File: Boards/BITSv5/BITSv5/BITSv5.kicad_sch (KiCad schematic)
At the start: 81 parts, among them J1 Conn_01x10_Pin, J2 USB_C_Receptacle_USB2.0, J3 Conn_01x07, Q1 Q_NMOS_GSD, Q2 Q_PMOS_GSD, SW3 SLIDE, U1 MCU_RaspberryPi_RP2040_RP2040, U10 USBLC6-2SC6, U2 W25Q128JVS, U3 MAX-M10S, U4 MAX25255AFDA/VY+, U6 XBee_SMT, U7 TPS2121RUXR, U8 LT6703CDC-3, U9 TVS1800DRVR, Y1 12MHz

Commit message: small update to BITSv5 for review
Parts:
- removed R6: 1M, Resistor_SMD:R_0603_1608Metric_Pad0.98x0.95mm_HandSolder, symbol Device:R
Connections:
- net GND: now also J2.S1 (SHIELD)
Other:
- moved on the sheet: C26, C27, U6

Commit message: xbee joint and bits updates
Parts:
- R17: value 51.1K -> 46.4K
- R18: value 1.05M -> 1.5M
- R19: value 154K -> 100K
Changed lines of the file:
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@@
       (effects (font (size 1.27 1.27)) (justify left))
     )
-    (property "Value" "1.05M" (at 259.08 33.02 0)
+    (property "Value" "1.5M" (at 259.08 33.02 0)
       (effects (font (size 1.27 1.27)) (justify left))
     )
@@
       (effects (font (size 1.27 1.27)) (justify left))
     )
-    (property "Value" "154K" (at 259.08 43.18 0)
+    (property "Value" "100K" (at 259.08 43.18 0)
       (effects (font (size 1.27 1.27)) (justify left))
     )
@@
       (effects (font (size 1.27 1.27)) (justify left))
     )
-    (property "Value" "51.1K" (at 45.72 262.89 0)
-      (effects (font (size 1.27 1.27)) (justify left))
-    )
+    (property "Value" "46.4K" (at 45.72 262.89 0)
+      (effects (font (size 1.27 1.27)) (justify left))
+    )

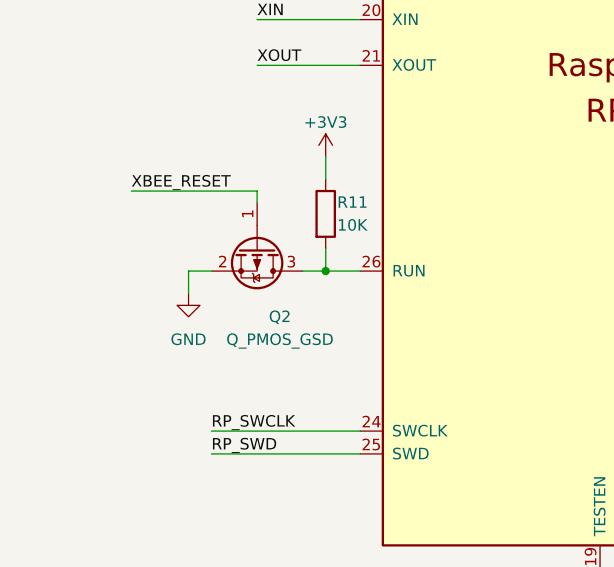
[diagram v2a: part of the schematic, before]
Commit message: added button to BITS5
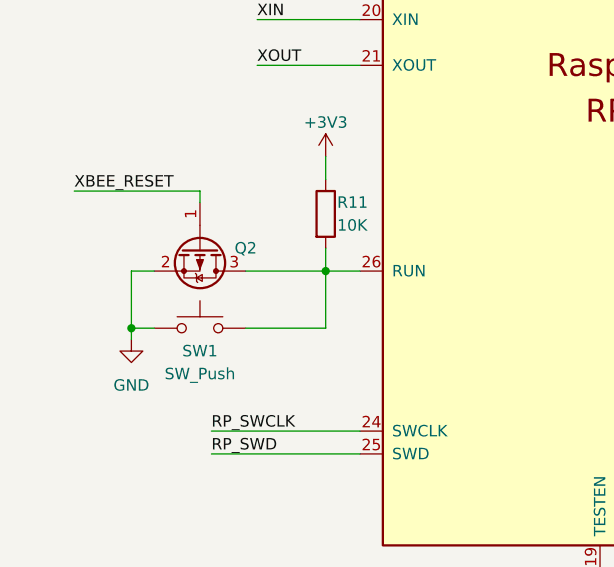
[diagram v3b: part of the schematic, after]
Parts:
- added SW1: SW_Push, Button_Switch_SMD:SW_Push_1P1T-SH_NO_CK_KMR2xxG, symbol Switch:SW_Push
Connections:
- net GND: now also SW1.1
- net at Q2.3 (D), R11.2, U1.26 (RUN): now also SW1.2
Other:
- moved on the sheet: Q2
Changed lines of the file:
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@@
   (junction (at 49.53 21.59) (diameter 0) (color 0 0 0 0)
   )
+  (junction (at 20.32 111.76) (diameter 0) (color 0 0 0 0)
+  )
   (junction (at 142.24 21.59) (diameter 0) (color 0 0 0 0)
   )
@@
     (stroke (width 0) (type default))
   )
-  (wire (pts (xy 29.21 105.41) (xy 26.67 105.41))
+  (wire (pts (xy 22.86 105.41) (xy 20.32 105.41))
     (stroke (width 0) (type default))
   )
@@
     (stroke (width 0) (type default))
   )
+  (wire (pts (xy 33.02 111.76) (xy 41.91 111.76))
+    (stroke (width 0) (type default))
+  )
   (wire (pts (xy 287.02 191.77) (xy 297.18 191.77))
     (stroke (width 0) (type default))
@@
     (stroke (width 0) (type default))
   )
-  (wire (pts (xy 34.29 96.52) (xy 20.32 96.52))
+  (wire (pts (xy 27.94 96.52) (xy 13.97 96.52))
     (stroke (width 0) (type default))
   )
@@
     (stroke (width 0) (type default))
   )
-  (wire (pts (xy 39.37 105.41) (xy 41.91 105.41))
+  (wire (pts (xy 33.02 105.41) (xy 41.91 105.41))
     (stroke (width 0) (type default))
   )
@@
     (stroke (width 0) (type default))
   )
+  (wire (pts (xy 41.91 111.76) (xy 41.91 105.41))
+    (stroke (width 0) (type default))
+  )
   (wire (pts (xy 222.25 177.8) (xy 222.25 179.07))
     (stroke (width 0) (type default))
@@
     (stroke (width 0) (type dash_dot))
   )
-  (wire (pts (xy 26.67 105.41) (xy 26.67 107.95))
+  (wire (pts (xy 20.32 105.41) (xy 20.32 111.76))
     (stroke (width 0) (type default))
   )
@@
     (stroke (width 0) (type default))
   )
-  (wire (pts (xy 34.29 96.52) (xy 34.29 97.79))
+  (wire (pts (xy 27.94 96.52) (xy 27.94 97.79))
     (stroke (width 0) (type default))
   )
@@
     (stroke (width 0) (type default))
   )
+  (wire (pts (xy 20.32 113.03) (xy 20.32 111.76))
+    (stroke (width 0) (type default))
+  )
   (wire (pts (xy 248.92 255.27) (xy 248.92 256.54))
     (stroke (width 0) (type default))
@@
     (stroke (width 0) (type default))
   )
+  (wire (pts (xy 20.32 111.76) (xy 22.86 111.76))
+    (stroke (width 0) (type default))
+  )
   (wire (pts (xy 363.22 33.02) (xy 364.49 33.02))
     (stroke (width 0) (type default))
@@
     (effects (font (size 1.27 1.27)) (justify left bottom))
   )
-  (label "XBEE_RESET" (at 20.32 96.52 0) (fields_autoplaced)
+  (label "XBEE_RESET" (at 13.97 96.52 0) (fields_autoplaced)
     (effects (font (size 1.27 1.27)) (justify left bottom))
   )
@@
     )
   )
-  (symbol (lib_id "power:GND") (at 26.67 107.95 0) (unit 1)
+  (symbol (lib_id "power:GND") (at 20.32 113.03 0) (unit 1)
     (in_bom yes) (on_board yes) (dnp no) (fields_autoplaced)
-    (property "Reference" "#PWR038" (at 26.67 114.3 0)
+    (property "Reference" "#PWR038" (at 20.32 119.38 0)
       (effects (font (size 1.27 1.27)) hide)
     )
-    (property "Value" "GND" (at 26.67 113.03 0)
+    (property "Value" "GND" (at 20.32 118.11 0)
       (effects (font (size 1.27 1.27)))
     )
-    (property "Footprint" "" (at 26.67 107.95 0)
+    (property "Footprint" "" (at 20.32 113.03 0)
       (effects (font (size 1.27 1.27)) hide)
     )
-    (property "Datasheet" "" (at 26.67 107.95 0)
+    (property "Datasheet" "" (at 20.32 113.03 0)
       (effects (font (size 1.27 1.27)) hide)
     )
@@
     )
   )
-  (symbol (lib_id "Device:Q_PMOS_GSD") (at 34.29 102.87 270) (unit 1)
+  (symbol (lib_id "Device:Q_PMOS_GSD") (at 27.94 102.87 270) (unit 1)
     (in_bom yes) (on_board yes) (dnp no)
-    (property "Reference" "Q2" (at 36.83 110.49 90)
+    (property "Reference" "Q2" (at 33.02 102.87 90)
       (effects (font (size 1.27 1.27)))
     )
-    (property "Value" "Q_PMOS_GSD" (at 36.83 113.03 90)
-      (effects (font (size 1.27 1.27)))
+    (property "Value" "Q_PMOS_GSD" (at 30.48 90.17 90)
+      (effects (font (size 1.27 1.27)) hide)
     )
-    (property "Footprint" "Package_TO_SOT_SMD:SOT-23" (at 36.83 107.95 0)
+    (property "Footprint" "Package_TO_SOT_SMD:SOT-23" (at 30.48 107.95 0)
       (effects (font (size 1.27 1.27)) hide)
     )
-    (property "Datasheet" "~" (at 34.29 102.87 0)
+    (property "Datasheet" "~" (at 27.94 102.87 0)
       (effects (font (size 1.27 1.27)) hide)
     )
@@
         )
       )
+    )
+  )
+  (symbol (lib_id "Switch:SW_Push") (at 27.94 111.76 0) (unit 1)
+    (in_bom yes) (on_board yes) (dnp no)
+    (property "Reference" "SW1" (at 27.94 114.3 0)
+      (effects (font (size 1.27 1.27)))
+    )
+    (property "Value" "SW_Push" (at 27.94 116.84 0)
+      (effects (font (size 1.27 1.27)))
+    )
+    (property "Footprint" "Button_Switch_SMD:SW_Push_1P1T-SH_NO_CK_KMR2xxG" (at 27.94 106.68 0)
+      (effects (font (size 1.27 1.27)) hide)
+    )
+    (property "Datasheet" "~" (at 27.94 106.68 0)
+      (effects (font (size 1.27 1.27)) hide)
+    )
+    (pin "1")
+    (pin "2")
+    (instances
+      (project "BITSv5"
+        (path "/55a258d3-b7da-466a-a6cc-38d8142826fc"
+          (reference "SW1") (unit 1)
+        )
+      )

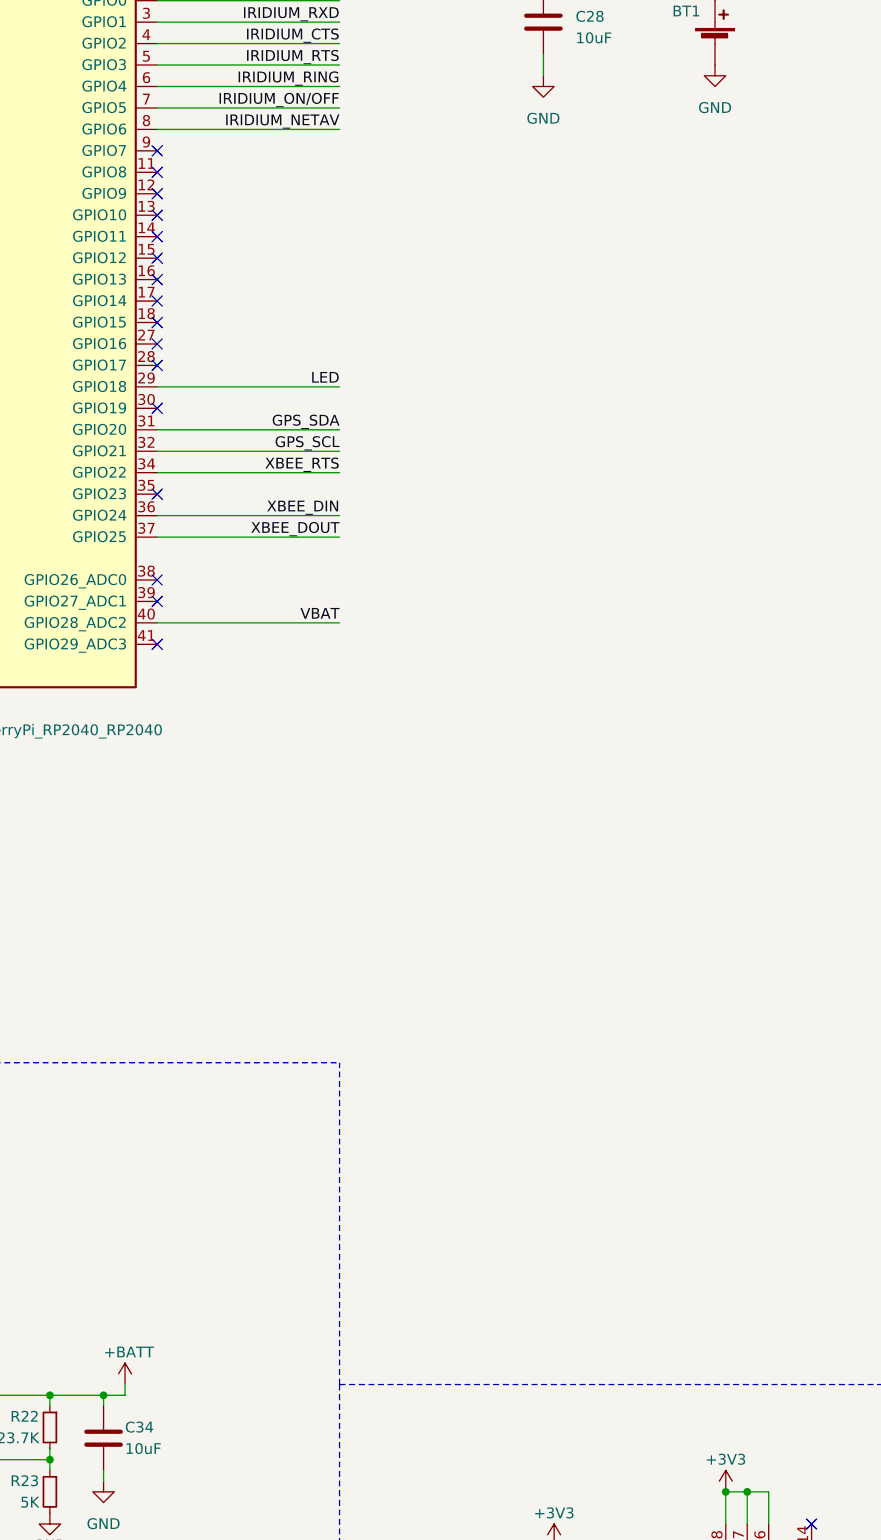
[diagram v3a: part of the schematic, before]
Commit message: BITSv5 added additional Xbee connector
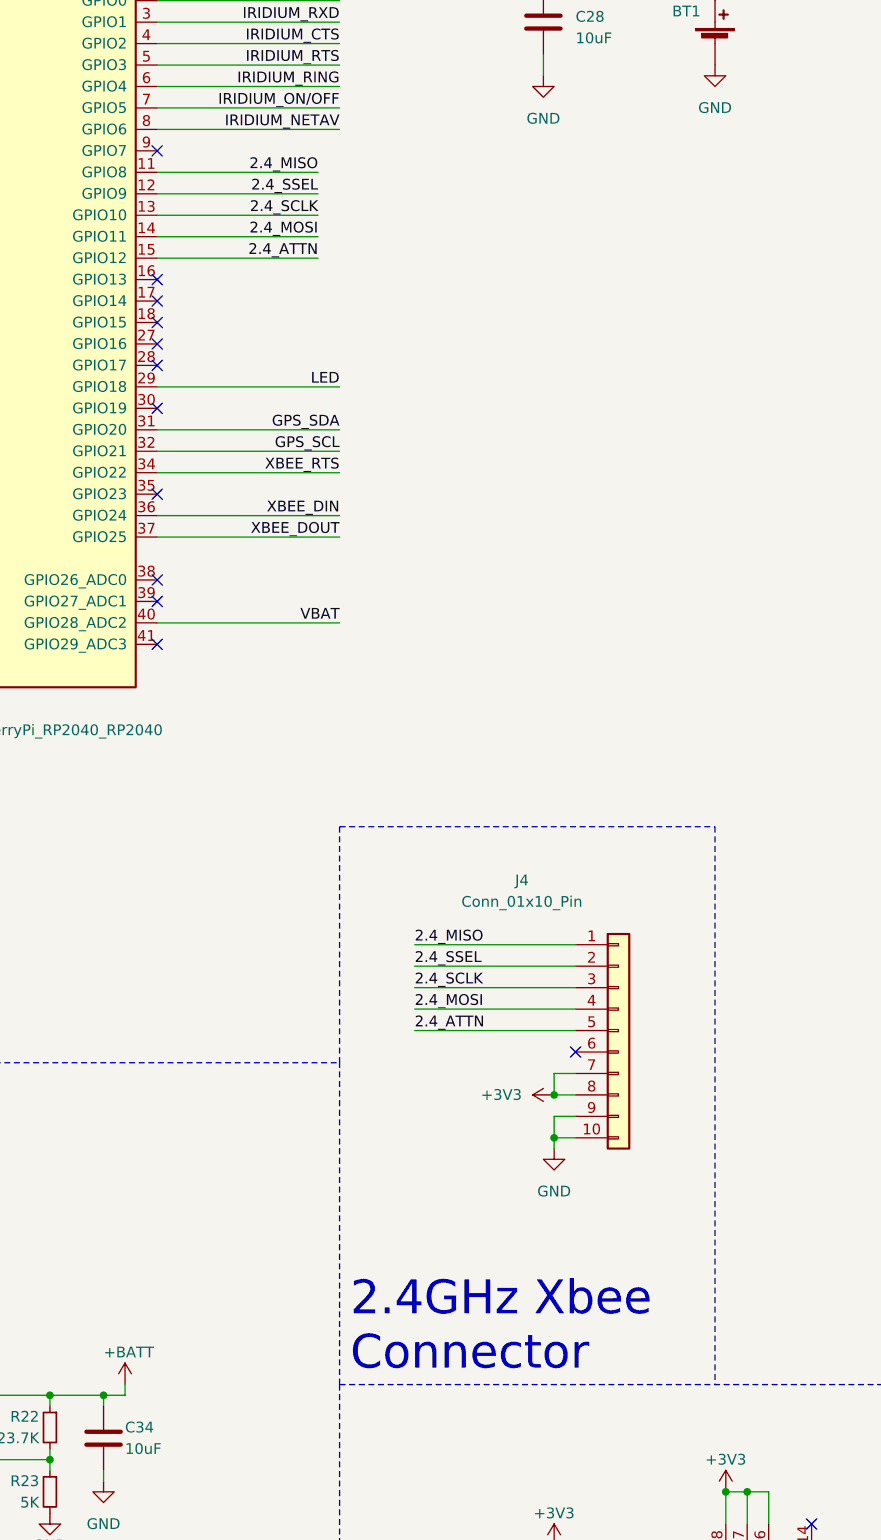
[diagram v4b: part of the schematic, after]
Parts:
- added J4: Conn_01x10_Pin, Connector_Molex:Molex_PicoBlade_53048-1010_1x10_P1.25mm_Horizontal, symbol Connector_Generic:Conn_01x10
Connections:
- net +3V3: now also J4.7 (Pin_7), J4.8 (Pin_8)
- net GND: now also J4.10 (Pin_10), J4.9 (Pin_9)
- net 2.4_MISO: now reaches U1.11 (GPIO8)
- net 2.4_MISO: now also J4.1 (Pin_1)
- net 2.4_SSEL: now reaches U1.12 (GPIO9)
- net 2.4_SSEL: now also J4.2 (Pin_2)
- net 2.4_SCLK: now reaches U1.13 (GPIO10)
- net 2.4_SCLK: now also J4.3 (Pin_3)
- net 2.4_MOSI: now reaches U1.14 (GPIO11)
- net 2.4_MOSI: now also J4.4 (Pin_4)
- net 2.4_ATTN: now reaches U1.15 (GPIO12)
- net 2.4_ATTN: now also J4.5 (Pin_5)
- no-connect marks 51 -> 47
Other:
- note added: "2.4GHz Xbee Connector"

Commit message: bits v5 w/ dorji radio
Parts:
- removed C17, C18, C19, C20, C21, C22: 22uF, Capacitor_SMD:C_0603_1608Metric_Pad1.08x0.95mm_HandSolder, symbol Device:C
- removed C23, C24: 0.1uF, Capacitor_SMD:C_0402_1005Metric_Pad0.74x0.62mm_HandSolder, symbol Device:C
- removed C26: 100pF, Capacitor_SMD:C_0603_1608Metric_Pad1.08x0.95mm_HandSolder, symbol Device:C
- removed C27: 1uF, Capacitor_SMD:C_0603_1608Metric_Pad1.08x0.95mm_HandSolder, symbol Device:C
- removed C28: 10uF, Capacitor_SMD:C_0603_1608Metric_Pad1.08x0.95mm_HandSolder, symbol Device:C
- removed C31: 0.1uF, Capacitor_SMD:C_0603_1608Metric_Pad1.08x0.95mm_HandSolder, symbol Device:C_Small
- removed J3: Conn_01x07, Connector_PinSocket_2.54mm:PinSocket_1x07_P2.54mm_Vertical, symbol Connector_Generic:Conn_01x07
- removed J4: Conn_01x10_Pin, Connector_Molex:Molex_PicoBlade_53048-1010_1x10_P1.25mm_Horizontal, symbol Connector_Generic:Conn_01x10
- removed L1, L2: 0.47uH, Inductor_SMD:L_1008_2520Metric_Pad1.43x2.20mm_HandSolder, symbol Device:L
- removed Q2: Q_PMOS_GSD, Package_TO_SOT_SMD:SOT-23, symbol Device:Q_PMOS_GSD
- removed R11: 10K, Resistor_SMD:R_0603_1608Metric_Pad0.98x0.95mm_HandSolder, symbol Device:R
- removed U4: MAX25255AFDA/VY+, BITSv5:21-100477_90-100168_MXM, symbol BITSv5:MAX25255DAFDG_VY+
- removed U6: XBee_SMT, BITSv5:XCVR_XBP9X-DMUS-001, symbol BITSv5:XBP9X-DMUS-001
- added AE2: Antenna, BITSv5:ANT_0915AT43A0026E_JOT, symbol Device:Antenna
- added BT2: 3V, BITSv5:SEIKO_ML414H_IV01E, symbol Device:Battery_Cell
- added C17, C23: 4.7pF, Capacitor_SMD:C_0603_1608Metric, symbol Device:C_Small
- added C18, C21: 470pF, Capacitor_SMD:C_0603_1608Metric, symbol Device:C_Small
- added C19, C24: 10nF, Capacitor_SMD:C_0603_1608Metric, symbol Device:C_Small
- added C20: 100uF, Capacitor_SMD:C_1206_3216Metric, symbol Device:C_Small
- added C22, C42: 100nF, Capacitor_SMD:C_0603_1608Metric, symbol Device:C_Small
- added C26: 10uF, Capacitor_SMD:C_0603_1608Metric, symbol Device:C_Small
- added C27, C39, C40, C41: 1uF, Capacitor_SMD:C_0603_1608Metric, symbol Device:C_Small
- added C28, C38: 15uF, Capacitor_SMD:C_1206_3216Metric, symbol Device:C_Small
- added C43: 200nF, Capacitor_SMD:C_0603_1608Metric, symbol Device:C_Small
- added D2: 0.5A/40V/240mV, Diode_SMD:D_SOD-123F, symbol Device:D_Schottky_Small
- added H1, H2, H4: M2, MountingHole:MountingHole_2.2mm_M2_Pad, symbol Mechanical:MountingHole
- added H3: M2, MountingHole:MountingHole_2.2mm_M2_Pad, symbol Mechanical:MountingHole_Pad
- added J3: SOICbite, BITSv5:SOIC_clipProgSmall, symbol Connector:Conn_01x08_Socket
- added L1, L2: 2.2uH, Inductor_SMD:L_1210_3225Metric, symbol Device:L_Small
- added L3, L4: 3.3uH, Inductor_SMD:L_1210_3225Metric, symbol Device:L_Small
- added R11, R29, R33: 100K, Resistor_SMD:R_0603_1608Metric, symbol Device:R_Small
- added R13: 100m, Resistor_SMD:R_0603_1608Metric, symbol Device:R_Small
- added R14: 3.3K, Resistor_SMD:R_0603_1608Metric, symbol Device:R_Small
- added R27: 22.1K, Resistor_SMD:R_0603_1608Metric, symbol Device:R_Small
- added R32: 34.8K, Resistor_SMD:R_0603_1608Metric, symbol Device:R_Small
- added R34: 15K, Resistor_SMD:R_0603_1608Metric, symbol Device:R_Small
- added R6: 10K, Resistor_SMD:R_0603_1608Metric, symbol Device:R_Small
- added U11: MS5607-02BA, Package_LGA:LGA-8_3x5mm_P1.25mm, symbol Sensor_Pressure:MS5607-02BA
- added U4: DRF1262TL, BITSv5:DRF1262TL, symbol BITSv5:DRF1262TL
- added U5: LT8653SIV-PBF, BITSv5:LT8653SIV-PBF, symbol BITSv5:LT8653SIV-PBF
- added U7: MAX6747KA29+T, 21-0078H_MXM, symbol BITSv5:MAX6747KA29+T
- C1, C10, C11, C2, C3, C32, C4, C5, C6, C7, C8, C9: footprint Capacitor_SMD:C_0402_1005Metric_Pad0.74x0.62mm_HandSolder -> Capacitor_SMD:C_0402_1005Metric; symbol Device:C -> Device:C_Small
- C12, C13, C14, C37: footprint Capacitor_SMD:C_0603_1608Metric_Pad1.08x0.95mm_HandSolder -> Capacitor_SMD:C_0402_1005Metric; symbol Device:C -> Device:C_Small
- C15: value 0.1uF -> 4.7uF; footprint Capacitor_SMD:C_0603_1608Metric_Pad1.08x0.95mm_HandSolder -> Capacitor_SMD:C_0603_1608Metric
- C16: value 4.7uF -> 47uF; footprint Capacitor_SMD:C_0603_1608Metric_Pad1.08x0.95mm_HandSolder -> Capacitor_SMD:C_1206_3216Metric
- C25: value 2.2uF -> 1uF; footprint Capacitor_SMD:C_0603_1608Metric_Pad1.08x0.95mm_HandSolder -> Capacitor_SMD:C_0603_1608Metric
- C29, C30: value 4.7uF -> 100nF; footprint Capacitor_SMD:C_0603_1608Metric_Pad1.08x0.95mm_HandSolder -> Capacitor_SMD:C_0603_1608Metric
- C33, C34, C35, C36: footprint Capacitor_SMD:C_0603_1608Metric_Pad1.08x0.95mm_HandSolder -> Capacitor_SMD:C_0603_1608Metric; symbol Device:C -> Device:C_Small
- J1: footprint Connector_Molex:Molex_PicoBlade_53048-1010_1x10_P1.25mm_Horizontal -> Connector_Molex:Molex_PicoBlade_53261-1071_1x10-1MP_P1.25mm_Horizontal
- J2: footprint Connector_USB:USB_C_Receptacle_GCT_USB4085 -> Connector_USB:USB_C_Receptacle_GCT_USB4105-xx-A_16P_TopMnt_Horizontal
- R1, R2: value 27Ω -> 27; footprint Resistor_SMD:R_0402_1005Metric_Pad0.72x0.64mm_HandSolder -> Resistor_SMD:R_0402_1005Metric; symbol Device:R -> Device:R_Small
- R10: value 10K -> 100m; footprint Resistor_SMD:R_0603_1608Metric_Pad0.98x0.95mm_HandSolder -> Resistor_SMD:R_0603_1608Metric
- R12, R21, R24, R4: footprint Resistor_SMD:R_0603_1608Metric_Pad0.98x0.95mm_HandSolder -> Resistor_SMD:R_0603_1608Metric; symbol Device:R -> Device:R_Small
- R15, R16, R22, R23, R9: footprint Resistor_SMD:R_0603_1608Metric_Pad0.98x0.95mm_HandSolder -> Resistor_SMD:R_0603_1608Metric
- R17: value 46.4K -> 44.2K; footprint Resistor_SMD:R_0603_1608Metric_Pad0.98x0.95mm_HandSolder -> Resistor_SMD:R_0603_1608Metric; symbol Device:R -> Device:R_Small
- R18, R19, R20: footprint Resistor_SMD:R_0603_1608Metric_Pad0.98x0.95mm_HandSolder -> Resistor_SMD:R_0402_1005Metric; symbol Device:R -> Device:R_Small
- R3: value 10K -> DNF; footprint Resistor_SMD:R_0603_1608Metric_Pad0.98x0.95mm_HandSolder -> Resistor_SMD:R_0603_1608Metric; symbol Device:R -> Device:R_Small
- R5: footprint Resistor_SMD:R_0402_1005Metric_Pad0.72x0.64mm_HandSolder -> Capacitor_SMD:C_0402_1005Metric; symbol Device:R -> Device:R_Small
- R7, R8: symbol Device:R -> Device:R_Small
- U1: symbol RP2040_minimal-cache:MCU_RaspberryPi_RP2040_RP2040 -> BITSv5:MCU_RaspberryPi_RP2040
- U10: footprint BITSv5:SOT23-6L_STM-M -> SOT23-6L_STM; symbol USBLC6-2SC6:USBLC6-2SC6 -> BITSv5:USBLC6-2SC6
- U2: footprint Package_SO:SOIC-8_5.23x5.23mm_P1.27mm -> BITSv5:WSON_128JVPIQ_WIN
- U6: renamed from U7; symbol TPS2121:TPS2121RUXR -> BITSv5:TPS2121RUXR
- Y1: symbol Device:Crystal_GND24 -> Device:Crystal_GND24_Small
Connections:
- net 2.4_ATTN is gone; now on net IRIDIUM_TXD: U1.15 (GPIO12)
- net GPS_SDA is gone; now on net SDA: R21.2, U1.31 (GPIO20), U3.16 (SDA)
- net +3V3: now also C29.1, R9.1, C28.1, C39.1, C41.1, D2.2 (A), L3.1, R11.1, R6.1, U11.1 (VDD), U11.2 (PS), U7.5 (WDS), U7.8 (VCC); no longer U3.6 (V_BCKP)
- net +5V: now also C26.1, C27.1, C38.1, L4.1, R13.1, U4.6 (VDD), U4.7 (VDD); no longer R9.1
- net GND: now also C13.2, C14.2, C15.2, C25.2, C29.2, C30.2, BT2.2 (-), C17.2, C18.2, C19.2, C20.2, C21.2, C22.2, C23.2, C24.2, C26.2, C27.2, C28.2, C38.2, C39.2, C40.2, C41.2, C42.2, C43.2, H3.1, J3.8 (Pin_8), R34.2, U11.3 (GND), U11.4 (CSB), U11.5 (CSB), U4.15 (GND), U4.17 (GND), U4.2 (GND), U4.4 (GND), U4.5 (GND), U5.21 (GND), U7.4 (GND); no longer C13.1, C14.1, C15.1, C25.1, C29.1, C30.1
- net IRIDIUM_NETAV: now also U1.6 (GPIO4); no longer U1.8 (GPIO6)
- net IRIDIUM_RING: now also U1.7 (GPIO5); no longer U1.6 (GPIO4)
- net IRIDIUM_TXD: no longer U1.2 (GPIO0)
- net LED: now also U1.2 (GPIO0); no longer U1.29 (GPIO18)
- net LVC_CUTOFF: now also U5.18 (EN/UV)
- net RP_SWCLK: now also J3.1 (Pin_1)
- net RP_SWD: now also J3.2 (Pin_2)
- net VCC: now also C15.1, C22.1, U5.19 (VIN), U5.20 (VIN), U5.5 (SYNC); no longer C15.2, C16.1, C29.2
- net at R5.1, Y1.1: now also C14.1; no longer C14.2
- net SDA: now reaches R9.2
- net SDA: now also U11.7 (SDI/SDA)
- net at SW1.2: now also C30.1, U7.1 (*MR); no longer U1.26 (RUN)
- net at R10.2: now also C20.1, L2.1, L3.2, R33.1, U5.10 (BIAS), U5.15 (FB2)
- net WATCHDOG: now reaches U1.16 (GPIO13)
- net WATCHDOG: now also U7.6 (WDI)
- net DRF_CLK: now reaches U1.38 (GPIO26_ADC0)
- net DRF_CLK: now also U4.13 (SCK)
- net DRF_MOSI: now reaches U1.39 (GPIO27_ADC1)
- net DRF_MOSI: now also U4.12 (MOSI)
- net 2.4_MISO renamed DRF_TXEN
- net DRF_TXEN: now also U4.3 (TXEN)
- net 2.4_MOSI renamed DRF_BUSY
- net DRF_BUSY: now also U4.9 (BUSY)
- net 2.4_SCLK renamed DRF_DIO1
- net DRF_DIO1: now also U4.8 (DIO1)
- net 2.4_SSEL renamed DRF_SW
- net DRF_SW: now also U4.1 (SW)
- net GPS_SCL renamed SCL
- net SCL: now also R6.2, U11.8 (SCLK)
- net IRIDIUM_ON/OFF renamed RESET
- net RESET: now also U1.26 (RUN), R11.2, U4.10 (RST), U7.7 (*RESET); no longer U1.7 (GPIO5)
- net VBAT: no longer names the net of U1.40 (GPIO28_ADC2)
- net XBEE_DIN renamed DRF_MISO
- net DRF_MISO: now also U4.11 (MISO)
- net XBEE_DOUT renamed DRF_CS
- net DRF_CS: now also U4.14 (NSS)
- net XBEE_RTS: no longer names the net of U1.34 (GPIO22)
- net XIN: no longer names the net of U1.20 (XIN), Y1.3
- net XIN: now also C13.1; no longer C13.2
- net XOUT: no longer names the net of R5.2, U1.21 (XOUT)
- new net: C17.1, R27.2, U5.11 (VC1)
- new net: D2.1 (K), R14.1
- new net: C25.1, U5.9 (VCC)
- new net: U3.10 (GND), U3.12 (GND)
- new net: BT2.1 (+), C40.1, R14.2, U3.6 (V_BCKP)
- new net: C42.1, U7.2 (SWT)
- new net: C43.1, U7.3 (SRT)
- new net: C18.1, R27.1
- new net: C21.1, R32.1
- new net: C23.1, R32.2, U5.16 (VC2)
- new net: C16.1, L1.1, L4.2, R13.2, R29.1, U5.12 (FB1)
- new net: C24.1, U5.14 (SS2)
- new net: AE2.1 (A), U4.16 (ANT)
- new net: R34.1, U5.17 (RT)
- new net: C19.1, U5.13 (SS1)
- new net: R33.2, U5.3 (PG2)
- new net: R29.2, U5.4 (PG1)
- new net: L1.2, U5.7 (SW1)
- new net: L2.2, U5.8 (SW2)
- no-connect marks 47 -> 34
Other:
- note added: "5V / 3.3V Buck Regulator"
- note added: "MCU"
- note added: "Power Multiplexer"
- note added: "Pressure and Temp. Sensor"
- note added: "Radio"
- note added: "RockBlock"
- note added: "SOICbite"
- note added: "USB C Plug"
- note added: "Voltage Clamps"
- note added: "Watchdog"
- note removed: "2.4GHz Xbee Connector"
- note removed: "Crystal"
- note removed: "Debug Headers"
- note removed: "Dual Buck Regulator"
- note removed: "Power Mux"
- note removed: "RockBlock Connector"
- note removed: "USB C Port"
- note removed: "XBee Pro SX 900"
- moved on the sheet: AE1, BT1, C1, C10, C11, C12, C13, C14, C2, C3, C32, C33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

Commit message: ordered new joint and bits
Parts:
- C17, C23: value 4.7pF -> 10pF
- C20: value 100uF -> 47uF
- C43: value 200nF -> 220nF
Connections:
- new net: U3.10 (GND), U3.12 (GND)
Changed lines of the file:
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@@
       (effects (font (size 1.27 1.27)))
     )
-    (property "Value" "4.7pF" (at 314.96 57.15 0)
+    (property "Value" "10pF" (at 314.96 57.15 0)
       (effects (font (size 1.27 1.27)))
     )
@@
       (effects (font (size 1.27 1.27)))
     )
-    (property "Value" "4.7pF" (at 358.14 57.15 0)
+    (property "Value" "10pF" (at 358.14 57.15 0)
       (effects (font (size 1.27 1.27)))
     )
@@
       (effects (font (size 1.27 1.27)))
     )
-    (property "Value" "200nF" (at 217.17 274.32 0)
+    (property "Value" "220nF" (at 217.17 274.32 0)
       (effects (font (size 1.27 1.27)))
     )
@@
       (effects (font (size 1.27 1.27)))
     )
-    (property "Value" "100uF" (at 384.81 34.29 0)
+    (property "Value" "47uF" (at 384.81 34.29 0)
       (effects (font (size 1.27 1.27)))
     )

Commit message: yep
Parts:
- removed J1: Conn_01x10_Pin, Connector_Molex:Molex_PicoBlade_53261-1071_1x10-1MP_P1.25mm_Horizontal, symbol Connector_Generic:Conn_01x10
- added J4: Conn_01x20, symbol Connector_Generic:Conn_01x20
- C17, C23: value 10pF -> 4.7pF
- J2: footprint Connector_USB:USB_C_Receptacle_GCT_USB4105-xx-A_16P_TopMnt_Horizontal -> Connector_USB:USB_C_Receptacle_GCT_USB4085
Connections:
- net +5V: now also J4.1 (Pin_1), J4.2 (Pin_2)
- net GND: now also J4.15 (Pin_15), J4.18 (Pin_18), J4.3 (Pin_3), J4.4 (Pin_4), J4.8 (Pin_8)
- net IRIDIUM_CTS: now also J4.11 (Pin_11)
- net IRIDIUM_NETAV: now also J4.19 (Pin_19)
- net IRIDIUM_RING: now also J4.12 (Pin_12)
- net IRIDIUM_RTS: now also J4.13 (Pin_13)
- net IRIDIUM_RXD: now also J4.7 (Pin_7)
- net IRIDIUM_TXD: now also J4.6 (Pin_6)
- new net: U3.10 (GND), U3.12 (GND)
- no-connect marks 34 -> 40

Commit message: starting BITSv5.1 hardware rev
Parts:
- removed C30, C42: 100nF, Capacitor_SMD:C_0603_1608Metric, symbol Device:C_Small
- removed C41: 1uF, Capacitor_SMD:C_0603_1608Metric, symbol Device:C_Small
- removed C43: 220nF, Capacitor_SMD:C_0603_1608Metric, symbol Device:C_Small
- removed R11: 100K, Resistor_SMD:R_0603_1608Metric, symbol Device:R_Small
- removed SW1: SW_Push, Button_Switch_SMD:SW_Push_1P1T-SH_NO_CK_KMR2xxG, symbol Switch:SW_Push
- removed U7: MAX6747KA29+T, 21-0078H_MXM, symbol BITSv5:MAX6747KA29+T
- R6, R9: value 10K -> DNF
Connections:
- net TIMEPULSE: now reaches U3.4 (TIMEPULSE)
- net TIMEPULSE: now also U1.29 (GPIO18)
- net EXTINT: now reaches U3.5 (EXTINT)
- net EXTINT: now also U1.28 (GPIO17)
- new net: U3.10 (GND), U3.12 (GND)
- no-connect marks 40 -> 36
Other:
- note removed: "Watchdog"
